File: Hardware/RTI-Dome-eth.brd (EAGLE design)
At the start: 119.4 x 71.2 mm, 86 parts, among them IC1 24AA128ST, IC3 FT232RL, IC4 REG1117, IC5 74LVC245, IC6 74ABT245, J1 POWERPOLE_POWER45A, U1 W5500, X13 PN61729-S, X9 J1011F21PNL

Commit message: Clenup
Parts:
- removed R9: 4.7K, rti:R0805
- R11: value 10K -> 4.7K
- moved R11 15.3 mm to (89.5, 56.7), turned to 0 degrees
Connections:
- removed net N$1: IC3.19, R11.1, R9.2
- new net FTDI_RESET: IC3.19, R11.1, U$1.23
- net USB_VCC: no longer R9.1
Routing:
- net FTDI_RESET: track 0.00 -> 29.7 mm, vias 0 -> 1
- net N$1: track 10.1 -> 0.00 mm
- net USB_VCC: track 3.08 -> 0.00 mm
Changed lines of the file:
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@@
 <attribute name="OC_FARNELL" value="1146032" x="106.68" y="82.55" size="1.778" layer="27" display="off"/>
 </element>
-<element name="R9" library="rti" package="R0805" value="4.7K" x="106.68" y="60.96" rot="R270">
-<attribute name="MPN" value="RT0805FRE074K7L" x="106.68" y="60.96" size="1.778" layer="27" rot="R270" display="off"/>
-</element>
-<element name="R11" library="rti" package="R0805" value="10K" x="104.14" y="60.96" rot="R90">
-<attribute name="MPN" value="RT0805FRE0710KL" x="104.14" y="60.96" size="1.778" layer="27" rot="R90" display="off"/>
+<element name="R11" library="rti" package="R0805" value="4.7K" x="89.46" y="56.7">
+<attribute name="MPN" value="RT0805FRE0710KL" x="89.46" y="56.7" size="1.778" layer="27" display="off"/>
 </element>
 <element name="X13" library="con-berg" package="PN61729-S" value="PN61729-S" x="114.3" y="60.96" rot="R90">
@@
 <via x="21.59" y="43.18" extent="1-16" drill="0.6" diameter="1.27"/>
 <via x="17.78" y="34.29" extent="1-16" drill="0.6" diameter="1.27"/>
-<via x="108.1405" y="57.94375" extent="1-16" drill="0.6" diameter="1.27"/>
+<via x="101.5255" y="61.40875" extent="1-16" drill="0.6" diameter="1.27"/>
 <via x="12.7" y="50.8" extent="1-16" drill="0.6" diameter="1.27"/>
 <contactref element="C3" pad="2"/>
@@
 <via x="26.67" y="3.81" extent="1-16" drill="0.6" diameter="1.27"/>
 <via x="73.66" y="38.1" extent="1-16" drill="0.6" diameter="1.27"/>
-<via x="91.44" y="39.37" extent="1-16" drill="0.6" diameter="1.27"/>
+<via x="91.44" y="40.945" extent="1-16" drill="0.6" diameter="1.27"/>
 <via x="94.0485" y="30.19175" extent="1-16" drill="0.6" diameter="1.27"/>
 <via x="94.185" y="25.2" extent="1-16" drill="0.6" diameter="1.27"/>
@@
 <via x="76.2" y="54.61" extent="1-16" drill="0.6" diameter="1.27"/>
 <via x="52.07" y="46.99" extent="1-16" drill="0.6" diameter="1.27"/>
-<via x="91.44" y="55.88" extent="1-16" drill="0.6" diameter="1.27"/>
+<via x="93.015" y="56.825" extent="1-16" drill="0.6" diameter="1.27"/>
 <via x="91.44" y="52.07" extent="1-16" drill="0.6" diameter="1.27"/>
 <via x="91.44" y="48.26" extent="1-16" drill="0.6" diameter="1.27"/>
@@
 <wire x1="18.19275" y1="58.07075" x2="18.19275" y2="59.27725" width="0.254" layer="16"/>
 </signal>
-<signal name="N$1">
-<contactref element="R9" pad="2"/>
-<contactref element="R11" pad="1"/>
-<contactref element="IC3" pad="19"/>
-<wire x1="104.14" y1="60.01" x2="106.68" y2="60.01" width="1.016" layer="1"/>
-<wire x1="108.305" y1="53.155" x2="108.305" y2="55.525" width="0.4064" layer="1"/>
-<wire x1="108.305" y1="55.525" x2="106.68" y2="57.15" width="0.4064" layer="1"/>
-<wire x1="106.68" y1="57.15" x2="106.68" y2="60.01" width="0.4064" layer="1"/>
-</signal>
 <signal name="USB_VCC">
 <contactref element="X13" pad="1"/>
-<contactref element="R9" pad="1"/>
-<wire x1="109.59" y1="62.21" x2="106.852" y2="62.21" width="1.016" layer="1"/>
-<wire x1="106.852" y1="62.21" x2="106.68" y2="61.91" width="1.016" layer="1"/>
 </signal>
 <signal name="USBDP">
@@
 <wire x1="104.515" y1="32.76" x2="105.41" y2="33.655" width="0.254" layer="1"/>
 </signal>
+<signal name="FTDI_RESET">
+<contactref element="U$1" pad="23"/>
+<contactref element="R11" pad="1"/>
+<contactref element="IC3" pad="19"/>
+<wire x1="85.75675" y1="56.73725" x2="91.31275" y2="56.73725" width="0.254" layer="16"/>
+<wire x1="91.31275" y1="56.73725" x2="97.02" y2="51.03" width="0.254" layer="16"/>
+<wire x1="97.02" y1="51.03" x2="108.045" y2="51.03" width="0.254" layer="16"/>
+<via x="108.045" y="51.03" extent="1-16" drill="0.3"/>
+<wire x1="108.045" y1="51.03" x2="108.305" y2="51.29" width="0.254" layer="1"/>
+<wire x1="108.305" y1="51.29" x2="108.305" y2="53.155" width="0.254" layer="1"/>
+<wire x1="88.51" y1="56.7" x2="88.47275" y2="56.73725" width="0.254" layer="1"/>
+<wire x1="88.47275" y1="56.73725" x2="85.75675" y2="56.73725" width="0.254" layer="1"/>
+</signal>
 </signals>

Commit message: The FTDI reset pull donw should bt 10K to make sure we can reset properly
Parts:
- R11: value 4.7K -> 10K
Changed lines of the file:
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@@
 <attribute name="OC_FARNELL" value="1146032" x="106.68" y="82.55" size="1.778" layer="27" display="off"/>
 </element>
-<element name="R11" library="rti" package="R0805" value="4.7K" x="89.46" y="56.7">
+<element name="R11" library="rti" package="R0805" value="10K" x="89.46" y="56.7">
 <attribute name="MPN" value="RT0805FRE0710KL" x="89.46" y="56.7" size="1.778" layer="27" display="off"/>
 </element>

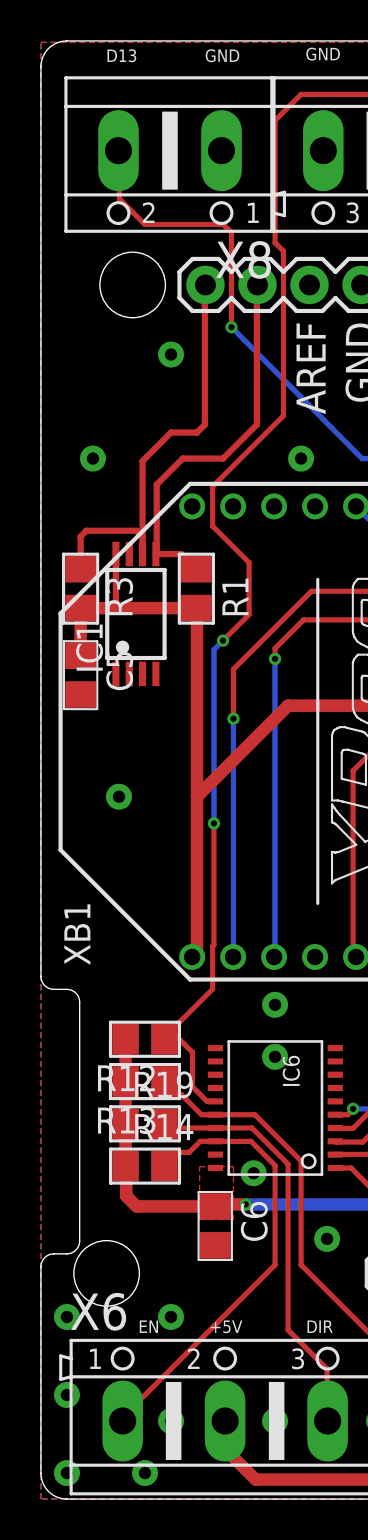
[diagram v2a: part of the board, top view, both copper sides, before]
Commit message: Change pin mode for better interrupt detection
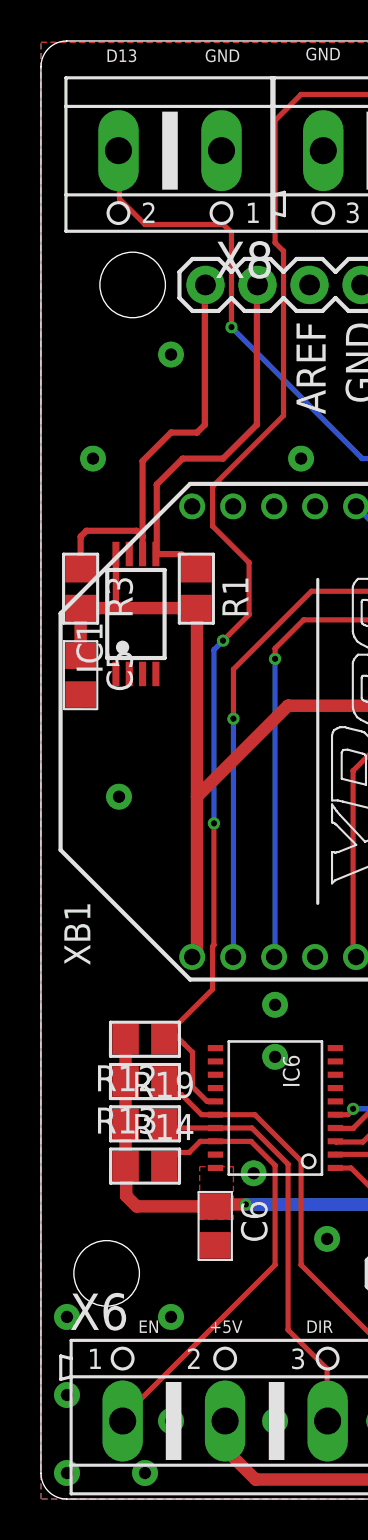
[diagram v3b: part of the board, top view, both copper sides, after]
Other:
- outline, holes or cut-outs redrawn
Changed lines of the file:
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@@
 <text x="48.26" y="3.81" size="1.778" layer="51">Dome Rotator</text>
 <hole x="100.99" y="19.105" drill="3.2"/>
-<wire x1="0" y1="1.26" x2="0" y2="11.34" width="0" layer="20"/>
-<wire x1="0" y1="11.34" x2="0.63" y2="11.97" width="0" layer="20" curve="-90"/>
-<wire x1="0.63" y1="11.97" x2="1.26" y2="11.97" width="0" layer="20"/>
-<wire x1="1.26" y1="11.97" x2="1.89" y2="12.6" width="0" layer="20" curve="90"/>
-<wire x1="1.89" y1="12.6" x2="1.89" y2="24.255" width="0" layer="20"/>
-<wire x1="1.89" y1="24.255" x2="1.26" y2="24.885" width="0" layer="20" curve="90"/>
-<wire x1="1.26" y1="24.885" x2="0.63" y2="24.885" width="0" layer="20"/>
-<wire x1="0.63" y1="24.885" x2="0" y2="25.515" width="0" layer="20" curve="-90"/>
-<wire x1="0" y1="25.515" x2="0" y2="69.93" width="0" layer="20"/>
 <wire x1="0" y1="69.93" x2="1.26" y2="71.19" width="0" layer="20" curve="-90"/>
 <wire x1="1.26" y1="71.19" x2="118.125" y2="71.19" width="0" layer="20"/>
@@
 <text x="25.225" y="0.55" size="0.6096" layer="22" rot="MR0">STEP</text>
 <text x="29.635" y="0.55" size="0.6096" layer="22" rot="MR0">+5V</text>
+<wire x1="0" y1="1.26" x2="0" y2="69.93" width="0" layer="20"/>
 </plain>
 <attributes>

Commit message: All recent update to pcb and code are in.
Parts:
- 25MHZ: device rti:CB3 -> rti:SMD-7050_4P
- X9: device rti:J1 -> rti:J1011F21PNL
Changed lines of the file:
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@@
 <layer number="220" name="220bmp" color="21" fill="1" visible="no" active="no"/>
 <layer number="221" name="221bmp" color="22" fill="1" visible="no" active="no"/>
-<layer number="222" name="222bmp" color="23" fill="1" visible="no" active="no"/>
 <layer number="223" name="223bmp" color="24" fill="1" visible="no" active="no"/>
 <layer number="224" name="224bmp" color="25" fill="1" visible="no" active="no"/>
@@
 <attribute name="MPN" value="RC0805FR-0749R9L" x="91.35" y="29.295" size="1.778" layer="27" rot="R180" display="off"/>
 </element>
-<element name="X9" library="rti" package="J1" value="J1011F21PNL" x="107.95" y="31.75" rot="R90">
+<element name="X9" library="rti" package="J1011F21PNL" value="J1011F21PNL" x="107.95" y="31.75" rot="R90">
 <attribute name="MF" value="" x="140.97" y="31.75" size="1.778" layer="27" rot="R90" display="off"/>
 <attribute name="MPN" value="J1011F21PNL" x="140.97" y="31.75" size="1.778" layer="27" rot="R90" display="off"/>
@@
 </element>
 <element name="J1" library="powerpoles" package="POWERPOLE_PAIR_45A" value="POWERPOLE_POWER45A" x="102.87" y="8.89" rot="MR90"/>
-<element name="25MHZ" library="rti" package="CB3" value="CB3LV-OSCILATOR" x="58.42" y="27.94">
+<element name="25MHZ" library="rti" package="SMD-7050_4P" value="CB3LV-OSCILATOR" x="58.42" y="27.94">
 <attribute name="MPN" value="CB3LV-3I-25M0000" x="58.42" y="27.94" size="1.778" layer="27" display="off"/>
 </element>

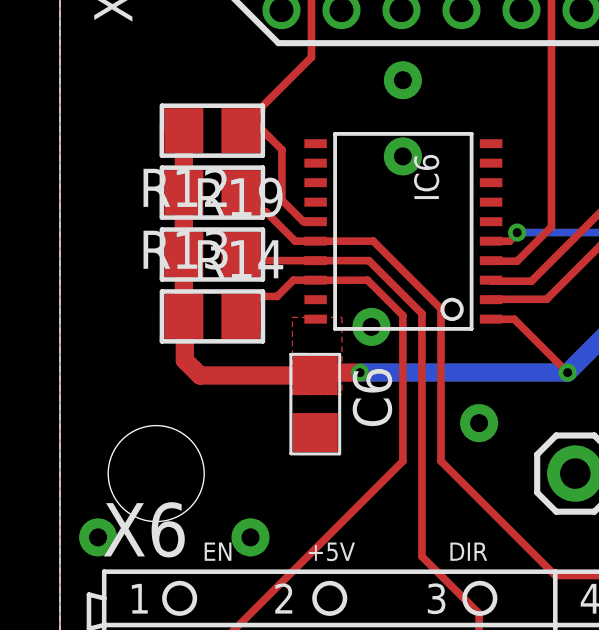
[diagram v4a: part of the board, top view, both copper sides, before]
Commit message: Re-did some of the core to receive data from network and wireless connection
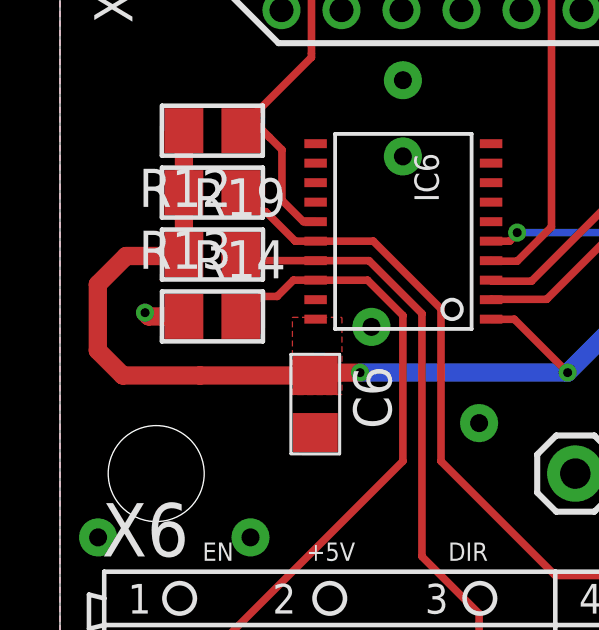
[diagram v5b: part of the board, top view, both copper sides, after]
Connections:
- net GND: now also R14.1
- net VCC: no longer R14.1
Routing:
- net VCC: track 134.2 -> 139.2 mm
- net GND: track 0.00 -> 1.35 mm, vias 94 -> 95
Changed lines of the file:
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@@
 <contactref element="X9" pad="M2"/>
 <contactref element="IC5" pad="P$19"/>
+<contactref element="R14" pad="1"/>
+<wire x1="4.13" y1="16.256" x2="2.959" y2="16.256" width="0.6096" layer="1"/>
+<wire x1="2.959" y1="16.256" x2="2.835" y2="16.38" width="0.6096" layer="1"/>
+<via x="2.835" y="16.38" extent="1-16" drill="0.3"/>
 </signal>
 <signal name="+12V" class="1">
@@
 <contactref element="R15" pad="1"/>
 <contactref element="R16" pad="1"/>
-<contactref element="R14" pad="1"/>
 <contactref element="R19" pad="1"/>
 <contactref element="R4" pad="2"/>
@@
 <wire x1="19.0246" y1="3.81" x2="19.0246" y2="0.9779" width="0.6096" layer="1"/>
 <wire x1="19.0246" y1="0.9779" x2="19.05" y2="0.9525" width="0.8128" layer="1"/>
-<wire x1="4.16175" y1="14.793" x2="4.66725" y2="14.2875" width="0.6096" layer="1"/>
 <wire x1="4.66725" y1="14.2875" x2="8.5065" y2="14.2875" width="0.6096" layer="1"/>
 <wire x1="8.5065" y1="14.2875" x2="8.509" y2="14.285" width="0.8128" layer="1"/>
 <contactref element="IC6" pad="P$20"/>
-<wire x1="4.16175" y1="14.793" x2="4.16175" y2="16.22425" width="0.6096" layer="1"/>
-<wire x1="4.16175" y1="16.22425" x2="4.13" y2="16.256" width="0.6096" layer="1"/>
-<wire x1="4.13" y1="16.256" x2="4.13" y2="18.31975" width="0.6096" layer="1"/>
 <wire x1="4.13" y1="20.3835" x2="3.8735" y2="20.3835" width="0.6096" layer="1"/>
 <wire x1="3.8735" y1="20.3835" x2="3.81" y2="20.32" width="0.6096" layer="1"/>
@@
 <wire x1="105.62975" y1="55.372" x2="105.62975" y2="57.54025" width="0.4064" layer="1"/>
 <wire x1="105.62975" y1="57.54025" x2="105.525" y2="57.645" width="0.4064" layer="1"/>
+<wire x1="4.66725" y1="14.2875" x2="2.0925" y2="14.2875" width="0.6096" layer="1"/>
+<wire x1="2.0925" y1="14.2875" x2="1.26" y2="15.12" width="0.6096" layer="1"/>
+<wire x1="1.26" y1="15.12" x2="1.26" y2="17.325" width="0.6096" layer="1"/>
+<wire x1="1.26" y1="17.325" x2="2.205" y2="18.27" width="0.6096" layer="1"/>
+<wire x1="2.205" y1="18.27" x2="4.08025" y2="18.27" width="0.6096" layer="1"/>
+<wire x1="4.08025" y1="18.27" x2="4.13" y2="18.31975" width="0.6096" layer="1"/>
 <wire x1="44.323" y1="27.879" x2="83.21675" y2="59.27725" width="0" layer="19" extent="1-1"/>
 </signal>

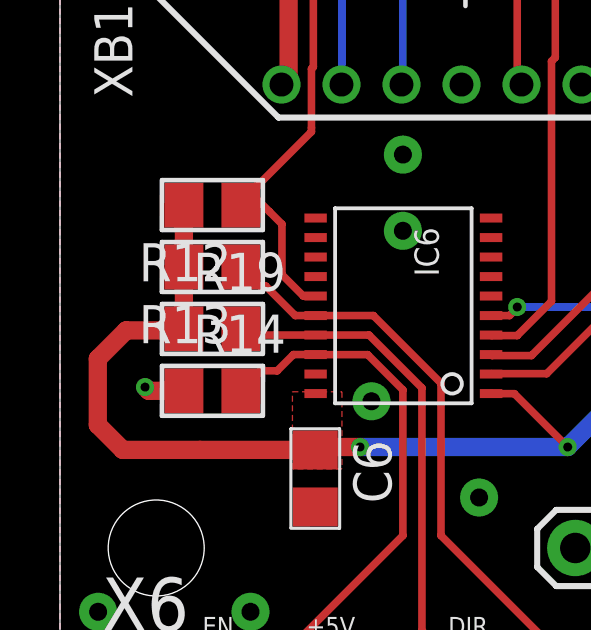
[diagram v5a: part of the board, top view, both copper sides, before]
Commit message: Making some pull-up pull-down to get a better OFF state when the controller is not powered but the stepper driver is.
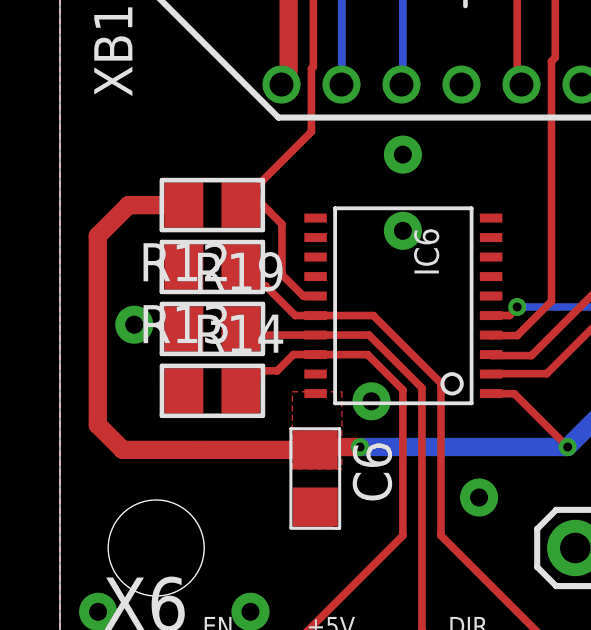
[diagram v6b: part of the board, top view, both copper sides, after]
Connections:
- net GND: now also R13.2, R19.1
- net VCC: no longer R13.2, R19.1
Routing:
- net GND: track 1.35 -> 0.00 mm
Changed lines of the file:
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@@
 <contactref element="IC5" pad="P$19"/>
 <contactref element="R14" pad="1"/>
-<wire x1="4.13" y1="16.256" x2="2.959" y2="16.256" width="0.6096" layer="1"/>
-<wire x1="2.959" y1="16.256" x2="2.835" y2="16.38" width="0.6096" layer="1"/>
-<via x="2.835" y="16.38" extent="1-16" drill="0.3"/>
+<contactref element="R13" pad="2"/>
+<contactref element="R19" pad="1"/>
+<via x="2.475" y="18.46" extent="1-16" drill="0.6" diameter="1.27"/>
 </signal>
 <signal name="+12V" class="1">
@@
 <signal name="VCC">
 <contactref element="R18" pad="1"/>
-<contactref element="R13" pad="2"/>
 <contactref element="R17" pad="1"/>
 <contactref element="R15" pad="1"/>
 <contactref element="R16" pad="1"/>
-<contactref element="R19" pad="1"/>
 <contactref element="R4" pad="2"/>
 <wire x1="27.305" y1="20.955" x2="29.21" y2="22.86" width="0.8128" layer="1"/>
@@
 <wire x1="8.5065" y1="14.2875" x2="8.509" y2="14.285" width="0.8128" layer="1"/>
 <contactref element="IC6" pad="P$20"/>
-<wire x1="4.13" y1="20.3835" x2="3.8735" y2="20.3835" width="0.6096" layer="1"/>
-<wire x1="3.8735" y1="20.3835" x2="3.81" y2="20.32" width="0.6096" layer="1"/>
-<wire x1="4.13" y1="18.31975" x2="4.13" y2="20.3835" width="0.6096" layer="1"/>
-<wire x1="4.13" y1="20.3835" x2="4.13" y2="22.44725" width="0.6096" layer="1"/>
 <wire x1="31.75" y1="27.879" x2="33.81375" y2="27.879" width="0.8128" layer="1"/>
 <wire x1="33.81375" y1="27.879" x2="35.8775" y2="27.879" width="0.8128" layer="1"/>
@@
 <wire x1="4.66725" y1="14.2875" x2="2.0925" y2="14.2875" width="0.6096" layer="1"/>
 <wire x1="2.0925" y1="14.2875" x2="1.26" y2="15.12" width="0.6096" layer="1"/>
-<wire x1="1.26" y1="15.12" x2="1.26" y2="17.325" width="0.6096" layer="1"/>
-<wire x1="1.26" y1="17.325" x2="2.205" y2="18.27" width="0.6096" layer="1"/>
-<wire x1="2.205" y1="18.27" x2="4.08025" y2="18.27" width="0.6096" layer="1"/>
-<wire x1="4.08025" y1="18.27" x2="4.13" y2="18.31975" width="0.6096" layer="1"/>
+<wire x1="4.13" y1="22.44725" x2="2.28725" y2="22.44725" width="0.6096" layer="1"/>
+<wire x1="2.28725" y1="22.44725" x2="1.26" y2="21.42" width="0.6096" layer="1"/>
+<wire x1="1.26" y1="21.42" x2="1.26" y2="15.12" width="0.6096" layer="1"/>
 <wire x1="44.323" y1="27.879" x2="83.21675" y2="59.27725" width="0" layer="19" extent="1-1"/>
 </signal>

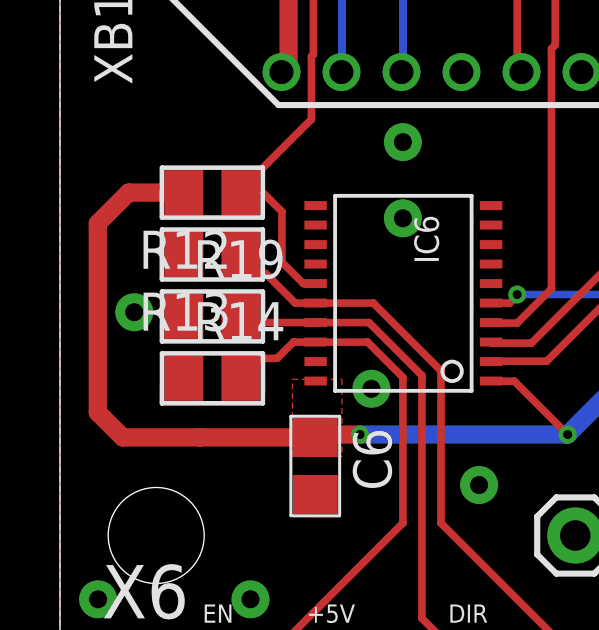
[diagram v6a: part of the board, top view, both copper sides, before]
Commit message: Pull-down doesn't really help. Setting back to pull-up to make sure enable does enable :)
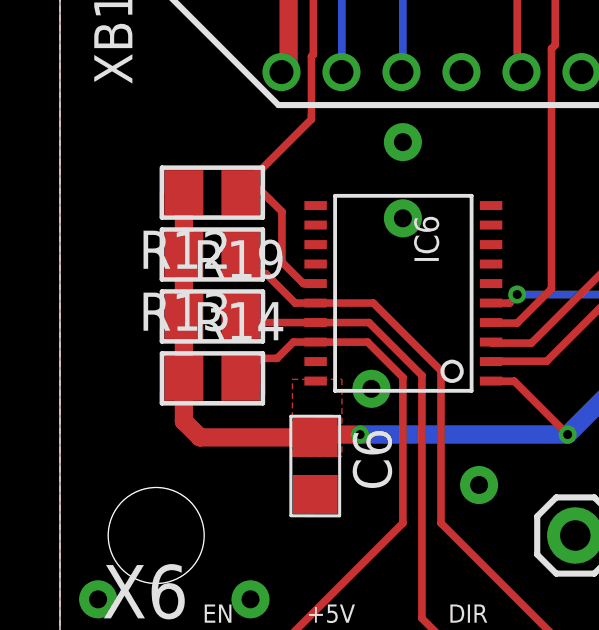
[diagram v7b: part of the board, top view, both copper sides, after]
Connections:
- net GND: no longer R13.2, R14.1, R19.1
- net VCC: now also R13.2, R14.1, R19.1
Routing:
- net VCC: track 138.8 -> 133.9 mm
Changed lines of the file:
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@@
 <contactref element="X9" pad="M2"/>
 <contactref element="IC5" pad="P$19"/>
-<contactref element="R14" pad="1"/>
-<contactref element="R13" pad="2"/>
-<contactref element="R19" pad="1"/>
-<via x="2.475" y="18.46" extent="1-16" drill="0.6" diameter="1.27"/>
 </signal>
 <signal name="+12V" class="1">
@@
 <wire x1="105.62975" y1="55.372" x2="105.62975" y2="57.54025" width="0.4064" layer="1"/>
 <wire x1="105.62975" y1="57.54025" x2="105.525" y2="57.645" width="0.4064" layer="1"/>
-<wire x1="4.66725" y1="14.2875" x2="2.0925" y2="14.2875" width="0.6096" layer="1"/>
-<wire x1="2.0925" y1="14.2875" x2="1.26" y2="15.12" width="0.6096" layer="1"/>
-<wire x1="4.13" y1="22.44725" x2="2.28725" y2="22.44725" width="0.6096" layer="1"/>
-<wire x1="2.28725" y1="22.44725" x2="1.26" y2="21.42" width="0.6096" layer="1"/>
-<wire x1="1.26" y1="21.42" x2="1.26" y2="15.12" width="0.6096" layer="1"/>
+<contactref element="R14" pad="1"/>
+<contactref element="R19" pad="1"/>
+<contactref element="R13" pad="2"/>
+<wire x1="4.66725" y1="14.2875" x2="4.13" y2="14.82475" width="0.6096" layer="1"/>
+<wire x1="4.13" y1="14.82475" x2="4.13" y2="16.256" width="0.6096" layer="1"/>
+<wire x1="4.13" y1="16.256" x2="4.13" y2="18.31975" width="0.6096" layer="1"/>
+<wire x1="4.13" y1="18.31975" x2="4.13" y2="20.3835" width="0.6096" layer="1"/>
+<wire x1="4.13" y1="20.3835" x2="4.13" y2="22.44725" width="0.6096" layer="1"/>
 <wire x1="44.323" y1="27.879" x2="83.21675" y2="59.27725" width="0" layer="19" extent="1-1"/>
 </signal>
